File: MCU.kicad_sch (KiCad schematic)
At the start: 36 parts, among them J4 Conn_01x04_Pin, J5 Conn_01x02_Pin, J7 Conn_01x02_Pin, Q6 S8050, Q7 S8050, Q8 S8050, SW1 SW_Push, U1 STM32F103C8Tx, Y1 8Mhz

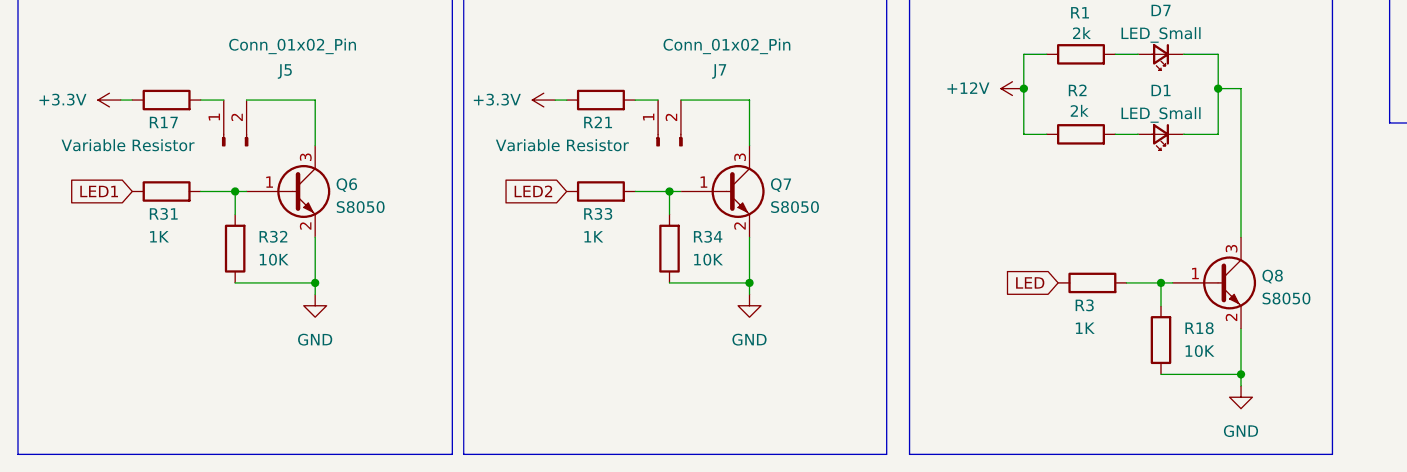
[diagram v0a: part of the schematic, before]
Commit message: Updated project structure and power traces
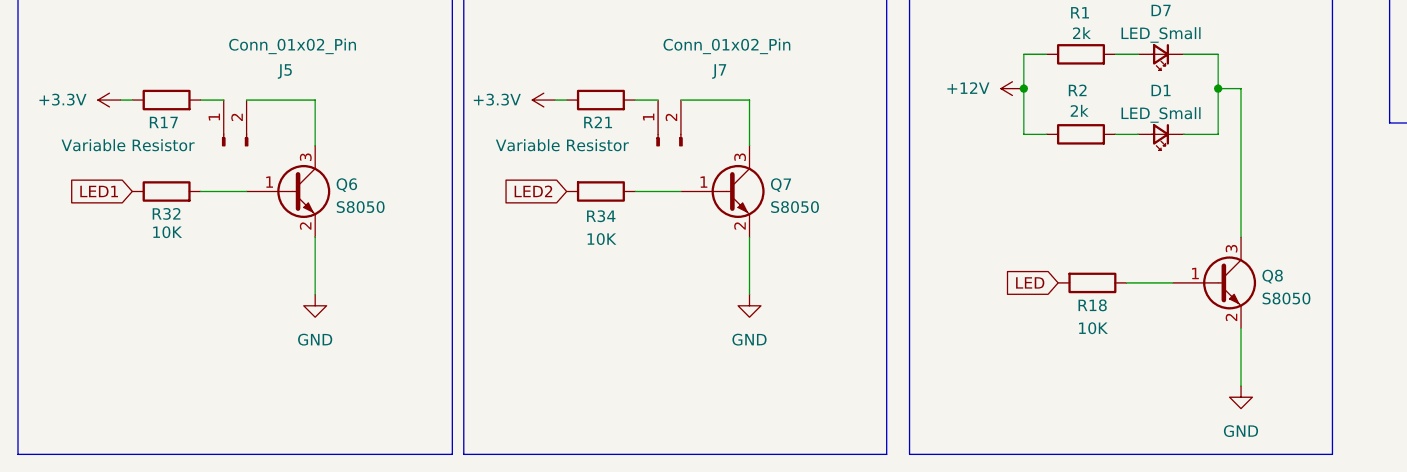
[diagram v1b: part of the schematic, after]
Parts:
- removed R3, R31, R33: 1K, Resistor_SMD:R_0603_1608Metric, symbol Device:R
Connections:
- net GND: no longer R18.1, R32.1, R34.1
- net LED: now also R18.2
- net LED1: now also R32.1
- net LED2: now also R34.2
- net at Q8.1 (B): now also R18.1; no longer R18.2
- net at Q7.1 (B): now also R34.1; no longer R34.2
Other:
- moved on the sheet: R18, R32, R34
